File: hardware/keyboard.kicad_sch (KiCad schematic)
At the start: 65 parts, among them SW1 SW_Push, SW10 SW_Push, SW11 SW_Push, SW12 SW_Push, SW13 SW_Push, SW14 SW_Push, SW15 SW_Push, SW16 SW_Push, SW17 SW_Push, SW18 SW_Push, SW19 SW_Push, SW2 SW_Push, SW20 SW_Push, SW21 SW_Push, SW22 SW_Push, SW23 SW_Push, SW24 SW_Push, SW25 SW_Push, SW26 SW_Push, SW27 SW_Push, SW28 SW_Push, SW29 SW_Push, SW3 SW_Push, SW30 SW_Push, SW31 SW_Push, SW32 SW_Push, SW33 SW_Push, SW34 SW_Push, SW35 SW_Push, SW36 SW_Push, SW37 SW_Push, SW38 SW_Push, SW39 SW_Push, SW4 SW_Push, SW40 SW_Push, SW41 SW_Push, SW42 SW_Push, SW43 SW_Push, SW44 SW_Push, SW45 SW_Push, SW46 SW_Push, SW47 SW_Push, SW48 SW_Push, SW49 SW_Push, SW5 SW_Push, SW50 SW_Push, SW51 SW_Push, SW52 SW_Push, SW53 SW_Push, SW54 SW_Push, SW55 SW_Push, SW56 SW_Push, SW6 SW_Push, SW7 SW_Push, SW8 SW_Push, SW9 SW_Push, U2 74HC138

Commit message: set footprints, some lcsc codes
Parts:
- R10, R11, R12, R13, R14, R15, R8, R9: footprint (none) -> Resistor_SMD:R_0603_1608Metric
- U2: footprint (none) -> Package_SO:SOIC-16_3.9x9.9mm_P1.27mm
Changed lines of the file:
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@@
 			)
 		)
-		(property "Footprint" ""
+		(property "Footprint" "Resistor_SMD:R_0603_1608Metric"
 			(at 83.82 126.238 90)
 			(effects
@@
 			)
 		)
-		(property "Footprint" ""
+		(property "Footprint" "Resistor_SMD:R_0603_1608Metric"
 			(at 83.82 113.538 90)
 			(effects
@@
 			)
 		)
-		(property "Footprint" ""
+		(property "Footprint" "Resistor_SMD:R_0603_1608Metric"
 			(at 83.82 123.698 90)
 			(effects
@@
 			)
 		)
-		(property "Footprint" ""
+		(property "Footprint" "Resistor_SMD:R_0603_1608Metric"
 			(at 83.82 118.618 90)
 			(effects
@@
 			)
 		)
-		(property "Footprint" ""
+		(property "Footprint" "Resistor_SMD:R_0603_1608Metric"
 			(at 83.82 110.998 90)
 			(effects
@@
 			)
 		)
-		(property "Footprint" ""
+		(property "Footprint" "Package_SO:SOIC-16_3.9x9.9mm_P1.27mm"
 			(at 67.31 119.38 0)
 			(effects
@@
 			)
 		)
-		(property "Footprint" ""
+		(property "Footprint" "Resistor_SMD:R_0603_1608Metric"
 			(at 83.82 121.158 90)
 			(effects
@@
 			)
 		)
-		(property "Footprint" ""
+		(property "Footprint" "Resistor_SMD:R_0603_1608Metric"
 			(at 83.82 116.078 90)
 			(effects
@@
 			)
 		)
-		(property "Footprint" ""
+		(property "Footprint" "Resistor_SMD:R_0603_1608Metric"
 			(at 83.82 128.778 90)
 			(effects

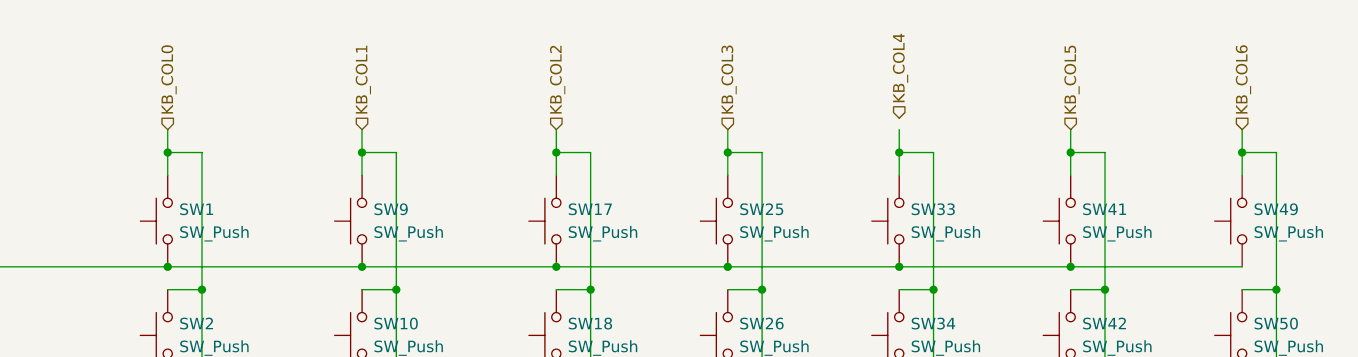
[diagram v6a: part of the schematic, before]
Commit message: lcd wires, wire direction
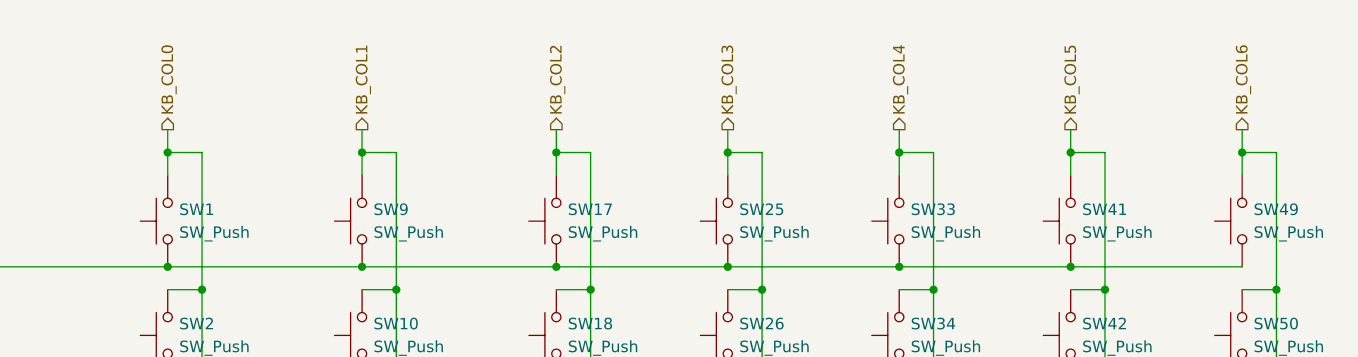
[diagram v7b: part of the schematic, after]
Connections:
- net KB_COL4: now also SW33.2, SW34.2, SW35.2, SW36.2, SW37.2, SW38.2, SW39.2, SW40.2
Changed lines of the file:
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@@
 	)
 	(hierarchical_label "KB_COL3"
-		(shape input)
+		(shape output)
 		(at 177.8 48.26 90)
 		(fields_autoplaced yes)
@@
 	)
 	(hierarchical_label "KB_COL2"
-		(shape input)
+		(shape output)
 		(at 158.75 48.26 90)
 		(fields_autoplaced yes)
@@
 	)
 	(hierarchical_label "KB_COL5"
-		(shape input)
+		(shape output)
 		(at 215.9 48.26 90)
 		(fields_autoplaced yes)
@@
 	)
 	(hierarchical_label "KB_COL6"
-		(shape input)
+		(shape output)
 		(at 234.95 48.26 90)
 		(fields_autoplaced yes)
@@
 	)
 	(hierarchical_label "KB_COL1"
-		(shape input)
+		(shape output)
 		(at 137.16 48.26 90)
 		(fields_autoplaced yes)
@@
 	)
 	(hierarchical_label "KB_COL0"
-		(shape input)
+		(shape output)
 		(at 115.57 48.26 90)
 		(fields_autoplaced yes)
@@
 	)
 	(hierarchical_label "KB_COL4"
-		(shape input)
-		(at 196.85 46.99 90)
+		(shape output)
+		(at 196.85 48.26 90)
 		(fields_autoplaced yes)
 		(effects

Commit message: display, switches, (switch)joystick footprint
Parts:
- SW1, SW10, SW11, SW12, SW13, SW14, SW15, SW16, SW17, SW18, SW19, SW2, SW20, SW21, SW22, SW23, SW24, SW25, SW26, SW27, SW28, SW29, SW3, SW30, SW31, SW32, SW33, SW34, SW35, SW36, SW37, SW38, SW39, SW4, SW40, SW41, SW42, SW43, SW44, SW45, SW46, SW47, SW48, SW49, SW5, SW50, SW51, SW52, SW53, SW54, SW55, SW56, SW6, SW7, SW8, SW9: footprint Button_Switch_SMD:SW_Push_1P1T_NO_6x6mm_H9.5mm -> lib:bottonepiccolo_C2888430
